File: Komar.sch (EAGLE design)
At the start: 108 parts, among them CON1 USB-VERTICAL, CON2 PINHEAD_1X01-2, CON3 CON-4P-TABS-STRAIGHT, CON4 CON-4P-TABS-STRAIGHT, CON5 CON-4P-TABS-STRAIGHT, CON6 CON-4P-TABS-STRAIGHT, CON7 CON-4P-TABS-STRAIGHT, CON8 CON-6P-SM06B, CON9 PINHEAD_1X01-2, IC1 TPD3S014DBVR-SOT23-6, IC2 TPD3S014DBVR-SOT23-6, IC3 ATA6561-GBQW-N-HVSON8, IC4 ATA6561-GBQW-N-HVSON8, IC5 MCP9700AT-E/TTVAO-SOT23, IC6 11LC040T-E/TT, Q1 FDMS86368-F085, Q10 FDMS86368-F085, Q11 FDMS86368-F085, Q12 FDMS86368-F085, Q2 FDMS86368-F085, Q3 FDMS86368-F085, Q4 FDMS86368-F085, Q5 FDMS86368-F085, Q6 FDMS86368-F085, Q7 FDMS86368-F085, Q8 FDMS86368-F085, Q9 FDMS86368-F085

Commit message: CAN transcievers rerouting
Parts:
- MODULE2: value MITOHONDRIQUE_V0.2-TH -> MITOCHONDRIK_LV-TH; device zubax_modules:MITOHONDRIQUE_V0.2-TH -> zubax_modules:MITOCHONDRIK_LV-TH
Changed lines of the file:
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@@
 </attributes>
 <variantdefs>
-<variantdef name="BASIC" current="yes"/>
+<variantdef name="BASIC"/>
 </variantdefs>
 <classes>
@@
 <attribute name="OPERATING_TEMP" value="-25°C ~ 85°C"/>
 </part>
-<part name="MODULE2" library="zubax_modules" library_urn="urn:adsk.eagle:library:5014895" deviceset="MITOHONDRIQUE_V0.2" device="-TH" package3d_urn="urn:adsk.eagle:package:4410646/13"/>
+<part name="MODULE2" library="zubax_modules" library_urn="urn:adsk.eagle:library:5014895" deviceset="MITOCHONDRIK_LV" device="-TH" package3d_urn="urn:adsk.eagle:package:4410646/15"/>
 <part name="IC6" library="misc" library_urn="urn:adsk.eagle:library:5347860" deviceset="11LC040T-E/TT" device="" package3d_urn="urn:adsk.eagle:package:1040193/4"/>
 <part name="GND44" library="supply_symbols" library_urn="urn:adsk.eagle:library:5017758" deviceset="GND" device="" value="GND"/>

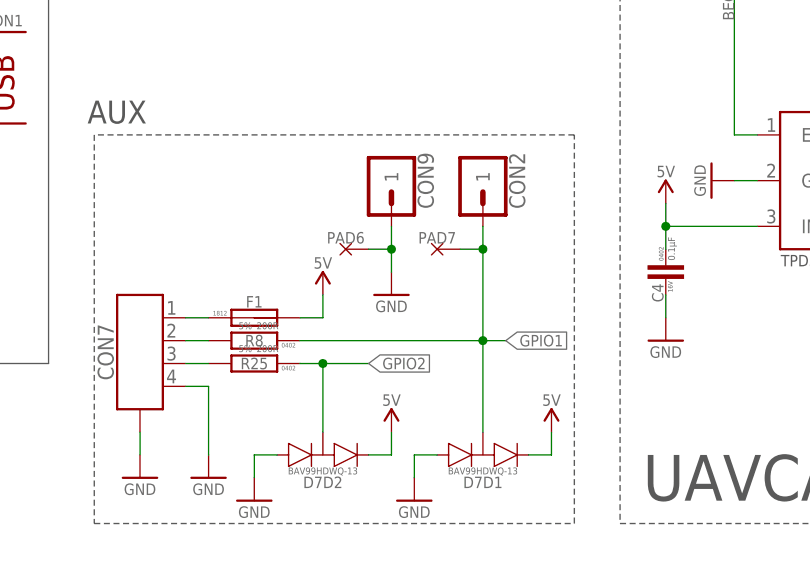
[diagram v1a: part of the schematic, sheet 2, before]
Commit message: Redundant thermistor pads removed
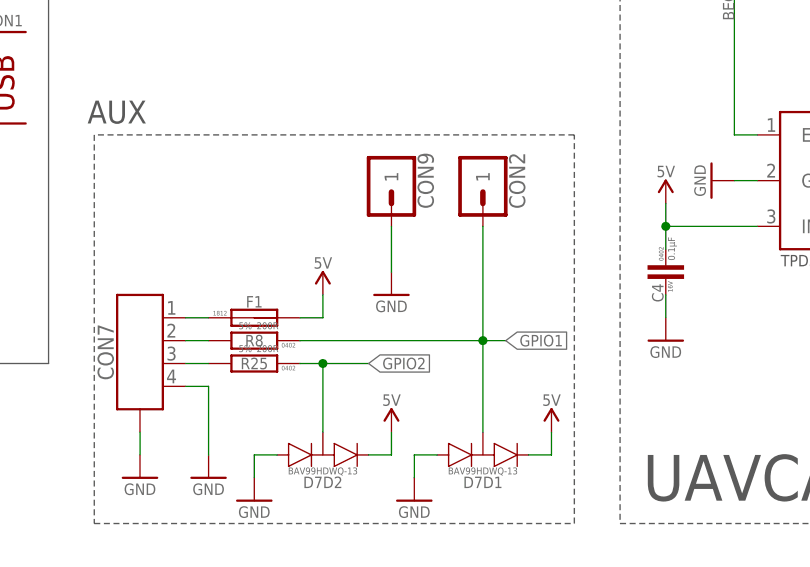
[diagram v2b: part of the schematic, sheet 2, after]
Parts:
- removed PAD6, PAD7: PAD-3X1.5, PADS:PAD-3X1.5
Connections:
- net GND: no longer PAD6.P$1
- net GPIO1: no longer PAD7.P$1
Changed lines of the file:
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@@
 </part>
 <part name="GND41" library="supply_symbols" library_urn="urn:adsk.eagle:library:5017758" deviceset="GND" device="" value="GND"/>
-<part name="PAD6" library="PADS" library_urn="urn:adsk.eagle:library:3188696" deviceset="PAD" device="-3X1.5" package3d_urn="urn:adsk.eagle:package:4854322/1">
-<variant name="BASIC" populate="no"/>
-</part>
-<part name="PAD7" library="PADS" library_urn="urn:adsk.eagle:library:3188696" deviceset="PAD" device="-3X1.5" package3d_urn="urn:adsk.eagle:package:4854322/1">
-<variant name="BASIC" populate="no"/>
-</part>
 <part name="C45" library="rc" library_urn="urn:adsk.eagle:library:2539423" deviceset="C" device="-1210" package3d_urn="urn:adsk.eagle:package:2539458/2" value="47µF">
 <attribute name="ASSY" value="DNM"/>
@@
 <attribute name="VALUE" x="213.36" y="54.61" size="1.27" layer="96" font="vector" ratio="15" align="center"/>
 </instance>
-<instance part="PAD6" gate="G$1" x="208.28" y="60.96" smashed="yes">
-<attribute name="NAME" x="208.28" y="62.23" size="1.27" layer="95" font="vector" ratio="15" align="center"/>
-</instance>
-<instance part="PAD7" gate="G$1" x="218.44" y="60.96" smashed="yes">
-<attribute name="NAME" x="218.44" y="62.23" size="1.27" layer="95" font="vector" ratio="15" align="center"/>
-</instance>
 <instance part="C45" gate="G$1" x="22.86" y="119.38" smashed="yes">
 <attribute name="ASSY" x="22.86" y="119.38" size="1.778" layer="96" display="off"/>
@@
 <pinref part="CON9" gate="G$1" pin="1"/>
 <pinref part="GND41" gate="1" pin="GND"/>
-<wire x1="213.36" y1="63.5" x2="213.36" y2="60.96" width="0.1524" layer="91"/>
-<pinref part="PAD6" gate="G$1" pin="P$1"/>
-<wire x1="213.36" y1="60.96" x2="213.36" y2="58.42" width="0.1524" layer="91"/>
-<wire x1="210.82" y1="60.96" x2="213.36" y2="60.96" width="0.1524" layer="91"/>
-<junction x="213.36" y="60.96"/>
+<wire x1="213.36" y1="63.5" x2="213.36" y2="58.42" width="0.1524" layer="91"/>
 </segment>
 <segment>
@@
 <junction x="223.52" y="50.8"/>
 <pinref part="CON2" gate="G$1" pin="1"/>
-<wire x1="223.52" y1="63.5" x2="223.52" y2="60.96" width="0.1524" layer="91"/>
-<pinref part="PAD7" gate="G$1" pin="P$1"/>
-<wire x1="223.52" y1="60.96" x2="223.52" y2="50.8" width="0.1524" layer="91"/>
-<wire x1="220.98" y1="60.96" x2="223.52" y2="60.96" width="0.1524" layer="91"/>
-<junction x="223.52" y="60.96"/>
-</segment>
-<segment>
+<wire x1="223.52" y1="63.5" x2="223.52" y2="50.8" width="0.1524" layer="91"/>
+</segment>
+<segment>

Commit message: minor attribute extension
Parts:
- F1: HOLD_CURRENT (none) -> 100 mA; TIME_TO_TRIP (none) -> 1.5 S; TRIP_CURRENT (none) -> 300 mA
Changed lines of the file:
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@@
 <attribute name="AEC-Q" value="AEC-Q200"/>
 <attribute name="DIGIKEY#" value="MF-MSMF010-2CT-ND"/>
+<attribute name="HOLD_CURRENT" value="100 mA"/>
 <attribute name="MANF" value="Bourns Inc."/>
 <attribute name="MANF#" value="MF-MSMF010-2"/>
+<attribute name="TIME_TO_TRIP" value="1.5 S"/>
+<attribute name="TRIP_CURRENT" value="300 mA"/>
 </part>
 <part name="R8" library="rc" library_urn="urn:adsk.eagle:library:2539423" deviceset="R" device="-0402" package3d_urn="urn:adsk.eagle:package:2539456/2" technology="-5%" value="200R">
@@
 <attribute name="OPERATING_TEMP" value="-25°C ~ 85°C"/>
 </part>
-<part name="MODULE2" library="zubax_modules" library_urn="urn:adsk.eagle:library:5014895" deviceset="MITOCHONDRIK_LV" device="-TH" package3d_urn="urn:adsk.eagle:package:4410646/15"/>
+<part name="MODULE2" library="zubax_modules" library_urn="urn:adsk.eagle:library:5014895" deviceset="MITOCHONDRIK_LV" device="-TH" package3d_urn="urn:adsk.eagle:package:4410646/16"/>
 <part name="IC6" library="misc" library_urn="urn:adsk.eagle:library:5347860" deviceset="11LC040T-E/TT" device="" package3d_urn="urn:adsk.eagle:package:1040193/4"/>
 <part name="GND44" library="supply_symbols" library_urn="urn:adsk.eagle:library:5017758" deviceset="GND" device="" value="GND"/>
@@
 <attribute name="NAME" x="198.12" y="55.118" size="1.27" layer="95" align="center"/>
 <attribute name="PACKAGE" x="194.31" y="53.848" size="0.508" layer="95" align="center"/>
+<attribute name="TIME_TO_TRIP" x="198.12" y="53.34" size="1.778" layer="96" font="vector" ratio="15" align="center" display="off"/>
+<attribute name="HOLD_CURRENT" x="198.12" y="53.34" size="1.778" layer="96" font="vector" ratio="15" align="center" display="off"/>
+<attribute name="TRIP_CURRENT" x="198.12" y="53.34" size="1.778" layer="96" font="vector" ratio="15" align="center" display="off"/>
 </instance>
 <instance part="R8" gate="G$1" x="198.12" y="50.8" smashed="yes" rot="R180">

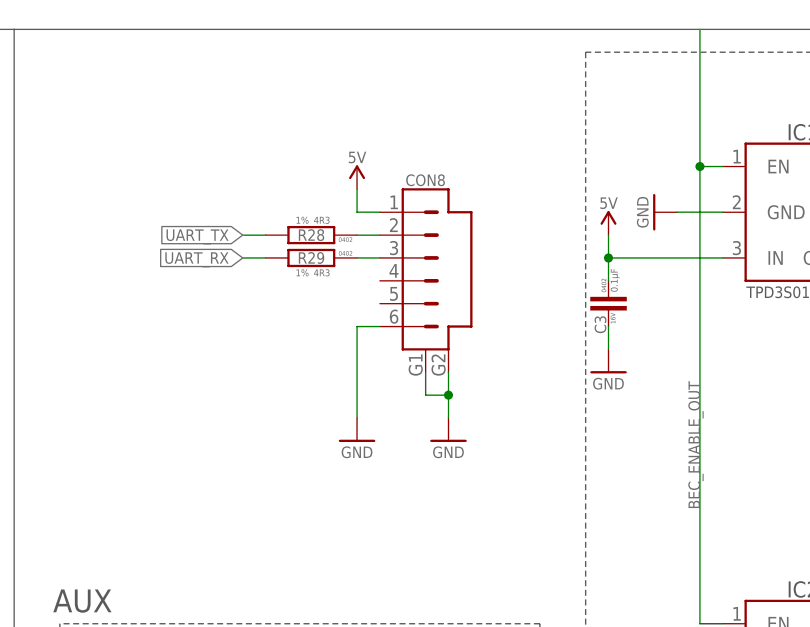
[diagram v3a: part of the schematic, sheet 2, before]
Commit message: CAN LEDs moved to other LEDs.
- DCP connector replaced with PLS-2 connector (marked DNM anyway)
- All LEDs moved 2 mm up
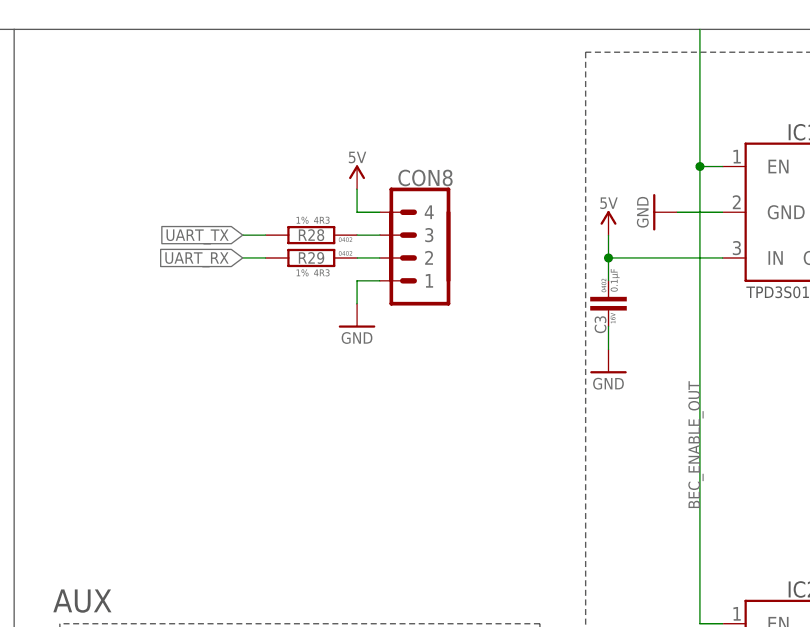
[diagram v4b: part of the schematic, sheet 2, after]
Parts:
- CON8: value CON-6P-SM06B -> PINHEAD_1X04-2; device Connectors:CON-6P-SM06B -> pinhead:PINHEAD_1X04-2
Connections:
- net GND: now also CON8.1; no longer CON8.6, CON8.G1, CON8.G2
- net N$25: now also CON8.3; no longer CON8.2
- net N$26: now also CON8.2; no longer CON8.3
- net VDD_5V: now also CON8.4; no longer CON8.1
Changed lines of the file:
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@@
 </attributes>
 <variantdefs>
-<variantdef name="BASIC"/>
+<variantdef name="BASIC" current="yes"/>
 </variantdefs>
 <classes>
@@
 <variant name="BASIC" populate="no"/>
 </part>
-<part name="CON8" library="Connectors" library_urn="urn:adsk.eagle:library:3750510" deviceset="CON-6P" device="-SM06B" package3d_urn="urn:adsk.eagle:package:1041174/4">
-<variant name="BASIC" populate="no"/>
-</part>
 <part name="+P16" library="supply_symbols" library_urn="urn:adsk.eagle:library:5017758" deviceset="5V" device=""/>
 <part name="CON2" library="pinhead" library_urn="urn:adsk.eagle:library:2540341" deviceset="PINHEAD_1X01" device="-2" package3d_urn="urn:adsk.eagle:package:2540397/3">
@@
 </part>
 <part name="+P25" library="supply_symbols" library_urn="urn:adsk.eagle:library:5017758" deviceset="5V" device=""/>
-<part name="GND46" library="supply_symbols" library_urn="urn:adsk.eagle:library:5017758" deviceset="GND" device="" value="GND"/>
 <part name="GND47" library="supply_symbols" library_urn="urn:adsk.eagle:library:5017758" deviceset="GND" device="" value="GND"/>
+<part name="CON8" library="pinhead" library_urn="urn:adsk.eagle:library:2540341" deviceset="PINHEAD_1X04" device="-2" package3d_urn="urn:adsk.eagle:package:4854340/3">
+<variant name="BASIC" populate="no"/>
+</part>
 </parts>
 <sheets>
@@
 <attribute name="TOLERANCE" x="208.026" y="112.268" size="0.762" layer="96" font="vector" rot="MR0"/>
 </instance>
-<instance part="CON8" gate="G$1" x="218.44" y="104.14" smashed="yes">
-<attribute name="NAME" x="220.98" y="122.936" size="1.27" layer="95" font="vector" ratio="15" align="center"/>
-</instance>
 <instance part="+P16" gate="G$1" x="213.36" y="121.92" smashed="yes">
 <attribute name="VALUE" x="213.36" y="125.476" size="1.27" layer="96" font="vector" ratio="15" align="center"/>
@@
 <attribute name="VALUE" x="106.68" y="39.116" size="1.27" layer="96" font="vector" ratio="15" rot="MR0" align="center"/>
 </instance>
-<instance part="GND46" gate="1" x="223.52" y="93.98" smashed="yes" rot="MR0">
-<attribute name="VALUE" x="223.52" y="92.71" size="1.27" layer="96" font="vector" ratio="15" rot="MR0" align="center"/>
-</instance>
-<instance part="GND47" gate="1" x="213.36" y="93.98" smashed="yes" rot="MR0">
-<attribute name="VALUE" x="213.36" y="92.71" size="1.27" layer="96" font="vector" ratio="15" rot="MR0" align="center"/>
+<instance part="GND47" gate="1" x="213.36" y="106.68" smashed="yes" rot="MR0">
+<attribute name="VALUE" x="213.36" y="105.41" size="1.27" layer="96" font="vector" ratio="15" rot="MR0" align="center"/>
+</instance>
+<instance part="CON8" gate="G$1" x="223.52" y="109.22" smashed="yes" rot="MR0">
+<attribute name="NAME" x="220.98" y="123.19" size="1.778" layer="95" font="vector" ratio="15" rot="MR0" align="center"/>
 </instance>
 </instances>
@@
 </segment>
 <segment>
-<pinref part="GND46" gate="1" pin="GND"/>
-<wire x1="220.98" y1="99.06" x2="223.52" y2="99.06" width="0.1524" layer="91"/>
-<wire x1="220.98" y1="101.6" x2="220.98" y2="99.06" width="0.1524" layer="91"/>
-<pinref part="CON8" gate="G$1" pin="G1"/>
-<pinref part="CON8" gate="G$1" pin="G2"/>
-<wire x1="223.52" y1="99.06" x2="223.52" y2="101.6" width="0.1524" layer="91"/>
-<wire x1="223.52" y1="96.52" x2="223.52" y2="99.06" width="0.1524" layer="91"/>
-<junction x="223.52" y="99.06"/>
-</segment>
-<segment>
 <pinref part="GND47" gate="1" pin="GND"/>
-<pinref part="CON8" gate="G$1" pin="6"/>
-<wire x1="215.9" y1="106.68" x2="213.36" y2="106.68" width="0.1524" layer="91"/>
-<wire x1="213.36" y1="106.68" x2="213.36" y2="96.52" width="0.1524" layer="91"/>
+<wire x1="213.36" y1="111.76" x2="213.36" y2="109.22" width="0.1524" layer="91"/>
+<pinref part="CON8" gate="G$1" pin="1"/>
+<wire x1="213.36" y1="111.76" x2="215.9" y2="111.76" width="0.1524" layer="91"/>
 </segment>
 </net>
@@
 </segment>
 <segment>
-<pinref part="CON8" gate="G$1" pin="1"/>
-<wire x1="215.9" y1="119.38" x2="213.36" y2="119.38" width="0.1524" layer="91"/>
 <wire x1="213.36" y1="119.38" x2="213.36" y2="121.92" width="0.1524" layer="91"/>
 <pinref part="+P16" gate="G$1" pin="VDD_5V"/>
+<pinref part="CON8" gate="G$1" pin="4"/>
+<wire x1="213.36" y1="119.38" x2="215.9" y2="119.38" width="0.1524" layer="91"/>
 </segment>
 <segment>
@@
 <net name="N$25" class="0">
 <segment>
-<pinref part="CON8" gate="G$1" pin="2"/>
 <pinref part="R28" gate="G$1" pin="1"/>
 <wire x1="213.36" y1="116.84" x2="215.9" y2="116.84" width="0.1524" layer="91"/>
+<pinref part="CON8" gate="G$1" pin="3"/>
 </segment>
 </net>
 <net name="N$26" class="0">
 <segment>
-<pinref part="CON8" gate="G$1" pin="3"/>
 <pinref part="R29" gate="G$1" pin="1"/>
 <wire x1="213.36" y1="114.3" x2="215.9" y2="114.3" width="0.1524" layer="91"/>
-</segment>
-</net>
+<pinref part="CON8" gate="G$1" pin="2"/>
+</segment>
+</net>

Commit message: Pins for lightpipes and capacitor support elements added
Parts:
- added CON10, CON11, CON12, CON13, CON14, CON15: PINHEAD_1X01-2, pinhead:PINHEAD_1X01-2
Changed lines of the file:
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@@
 </attributes>
 <variantdefs>
-<variantdef name="BASIC" current="yes"/>
+<variantdef name="BASIC"/>
 </variantdefs>
 <classes>
@@
 <variant name="BASIC" populate="no"/>
 </part>
+<part name="CON10" library="pinhead" library_urn="urn:adsk.eagle:library:2540341" deviceset="PINHEAD_1X01" device="-2" package3d_urn="urn:adsk.eagle:package:2540397/3"/>
+<part name="CON11" library="pinhead" library_urn="urn:adsk.eagle:library:2540341" deviceset="PINHEAD_1X01" device="-2" package3d_urn="urn:adsk.eagle:package:2540397/3"/>
+<part name="CON12" library="pinhead" library_urn="urn:adsk.eagle:library:2540341" deviceset="PINHEAD_1X01" device="-2" package3d_urn="urn:adsk.eagle:package:2540397/3"/>
+<part name="CON13" library="pinhead" library_urn="urn:adsk.eagle:library:2540341" deviceset="PINHEAD_1X01" device="-2" package3d_urn="urn:adsk.eagle:package:2540397/3"/>
+<part name="CON14" library="pinhead" library_urn="urn:adsk.eagle:library:2540341" deviceset="PINHEAD_1X01" device="-2" package3d_urn="urn:adsk.eagle:package:2540397/3"/>
+<part name="CON15" library="pinhead" library_urn="urn:adsk.eagle:library:2540341" deviceset="PINHEAD_1X01" device="-2" package3d_urn="urn:adsk.eagle:package:2540397/3"/>
 </parts>
 <sheets>
@@
 <attribute name="NAME" x="220.98" y="123.19" size="1.778" layer="95" font="vector" ratio="15" rot="MR0" align="center"/>
 </instance>
+<instance part="CON10" gate="G$1" x="264.16" y="7.62" smashed="yes" rot="R90">
+<attribute name="NAME" x="257.81" y="10.16" size="1.778" layer="95" font="vector" ratio="15" rot="R90" align="center"/>
+</instance>
+<instance part="CON11" gate="G$1" x="254" y="7.62" smashed="yes" rot="R90">
+<attribute name="NAME" x="247.65" y="10.16" size="1.778" layer="95" font="vector" ratio="15" rot="R90" align="center"/>
+</instance>
+<instance part="CON12" gate="G$1" x="241.3" y="7.62" smashed="yes" rot="R90">
+<attribute name="NAME" x="234.95" y="10.16" size="1.778" layer="95" font="vector" ratio="15" rot="R90" align="center"/>
+</instance>
+<instance part="CON13" gate="G$1" x="231.14" y="7.62" smashed="yes" rot="R90">
+<attribute name="NAME" x="224.79" y="10.16" size="1.778" layer="95" font="vector" ratio="15" rot="R90" align="center"/>
+</instance>
+<instance part="CON14" gate="G$1" x="220.98" y="7.62" smashed="yes" rot="R90">
+<attribute name="NAME" x="214.63" y="10.16" size="1.778" layer="95" font="vector" ratio="15" rot="R90" align="center"/>
+</instance>
+<instance part="CON15" gate="G$1" x="210.82" y="7.62" smashed="yes" rot="R90">
+<attribute name="NAME" x="204.47" y="10.16" size="1.778" layer="95" font="vector" ratio="15" rot="R90" align="center"/>
+</instance>
 </instances>
